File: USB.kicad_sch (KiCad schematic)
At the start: 15 parts, among them J201 USB1, U201 USB3320, U202 TPS76318

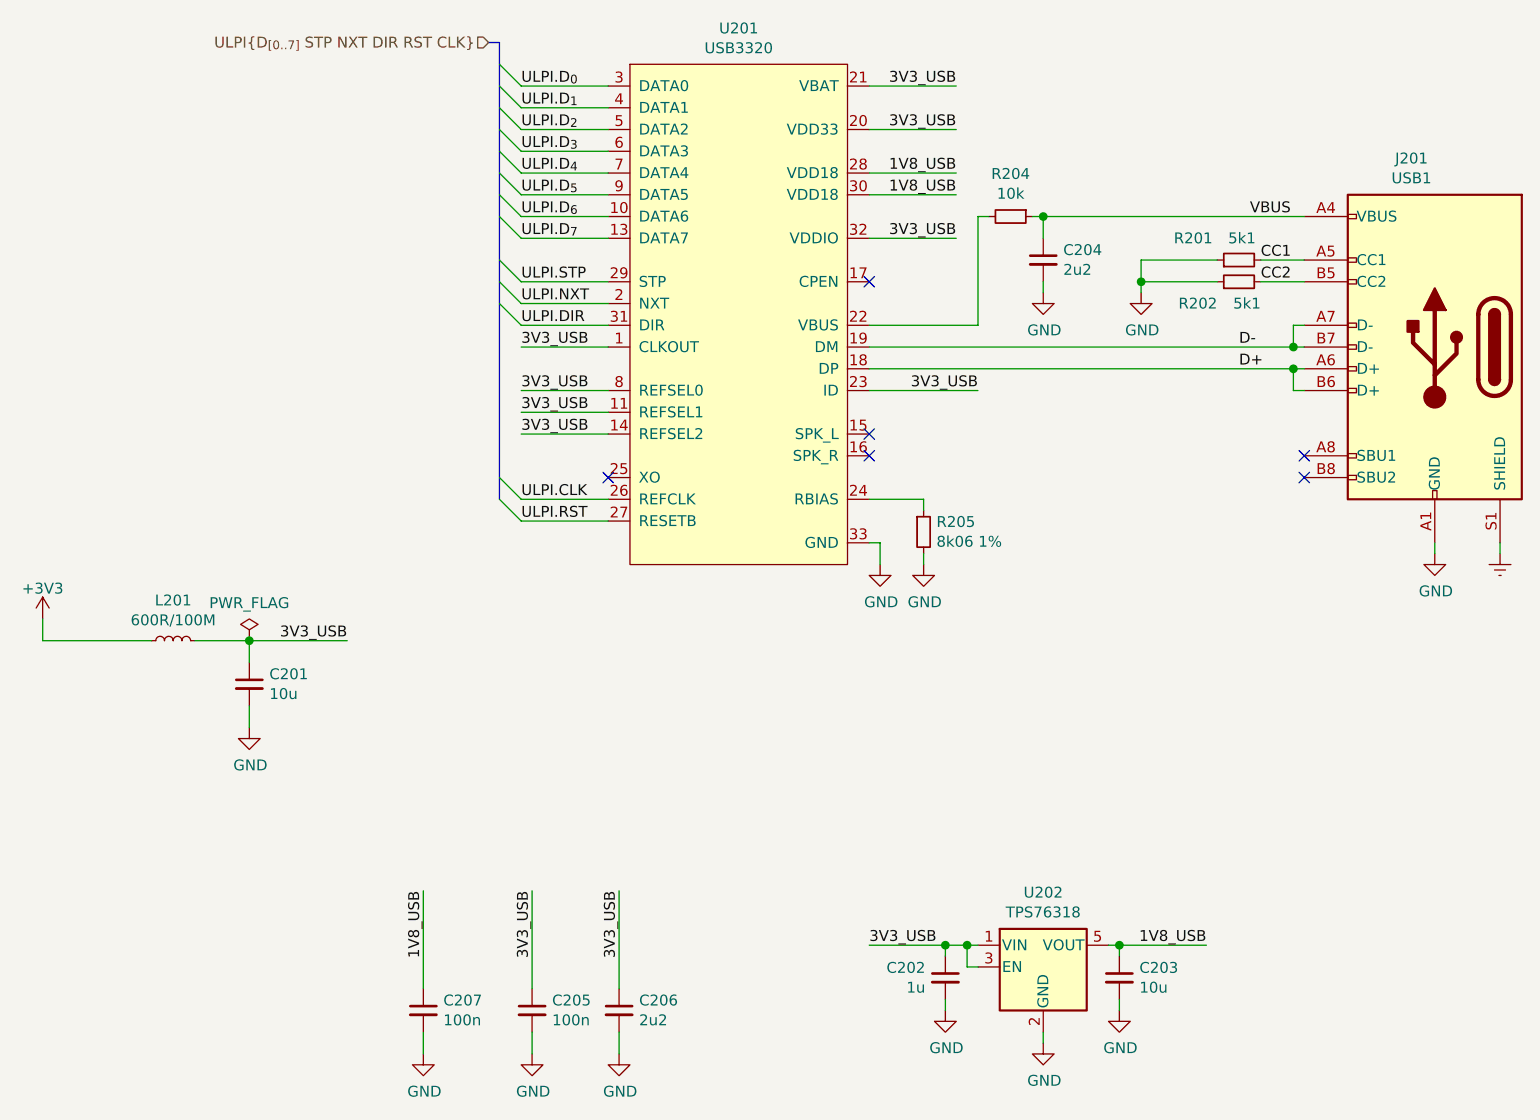
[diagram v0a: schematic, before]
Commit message: Update to KiCad 6
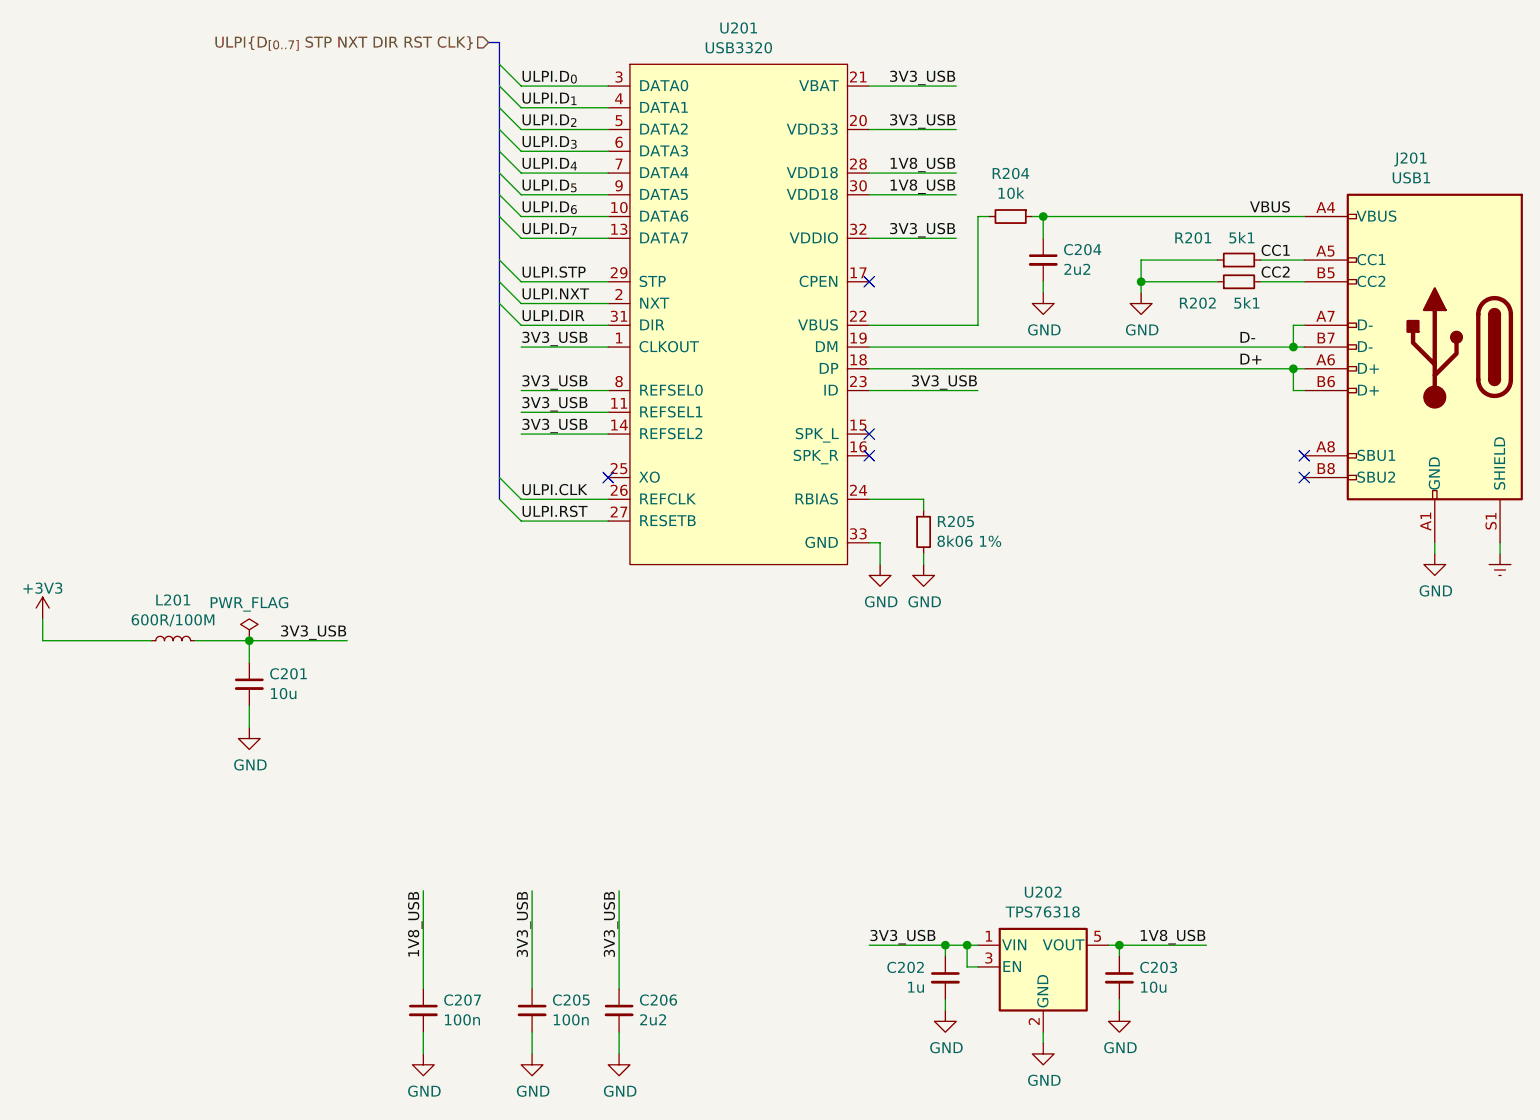
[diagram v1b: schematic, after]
